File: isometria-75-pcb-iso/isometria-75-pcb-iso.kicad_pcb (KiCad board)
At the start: 2 copper layers, 308.3 x 123 mm, 320 parts, among them J101 USB, J102 SPI, J103 Conn_01x01_Male, Q101 AO3400A, SW101 RST, SW102 BOOT, SW201 Rotary_Encoder_Switch, U101 XC6206P332MR, U102 STM32F072CBTx, U301 74LVC1G125

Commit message: matched usb trace length
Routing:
- net GND: track 804.1 -> 802.0 mm, vias 24 -> 23
- net USB-D-: track 21.5 -> 23.0 mm
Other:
- net class USB: trace_width 0.254 -> 0.1905
- rule trace_min: 0.254 -> 0.127

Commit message: some minor routing improvements
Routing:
- net ROW0: track 424.0 -> 427.9 mm
- net COL4: track 211.2 -> 209.9 mm
- net SPI_RES: track 24.3 -> 25.3 mm
- net LED-: track 1894.4 -> 1895.4 mm
- net COL1: track 255.9 -> 255.2 mm
- net COL6: track 175.1 -> 174.4 mm
- net COL3: track 232.7 -> 232.0 mm
- net COL2: track 244.5 -> 243.8 mm
- net COL5: track 163.4 -> 162.7 mm
- net COL12: track 196.2 -> 195.7 mm
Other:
- net class Power: trace_width 0.3048 -> 0.508

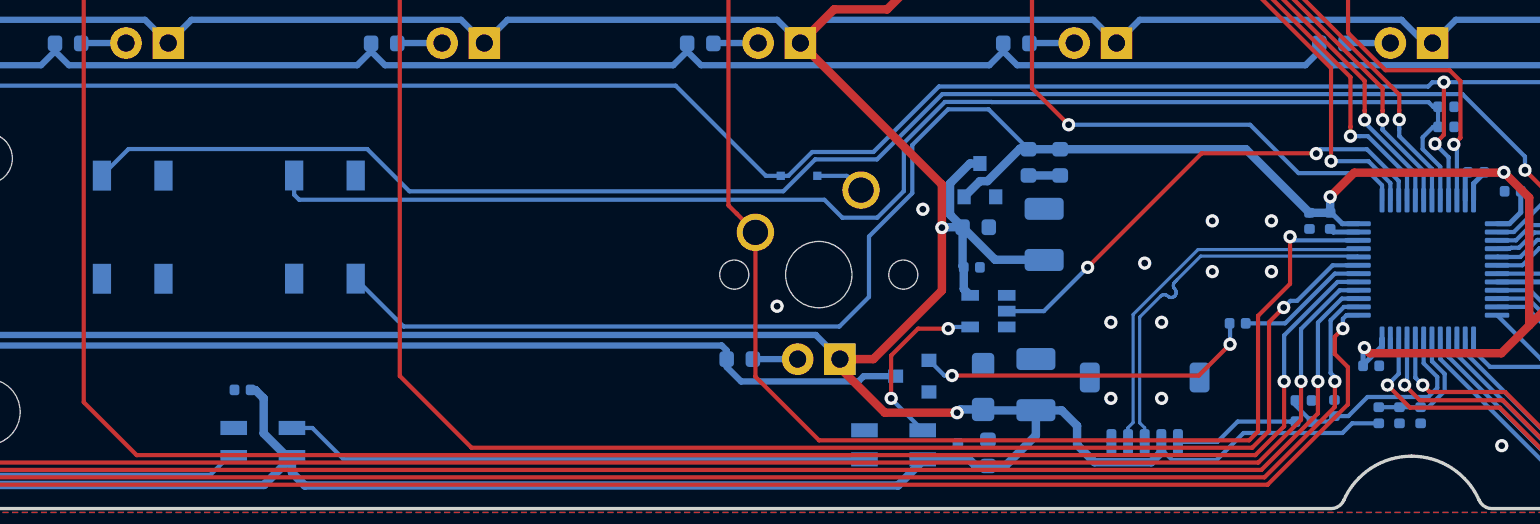
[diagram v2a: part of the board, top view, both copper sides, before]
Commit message: rerouted some traces
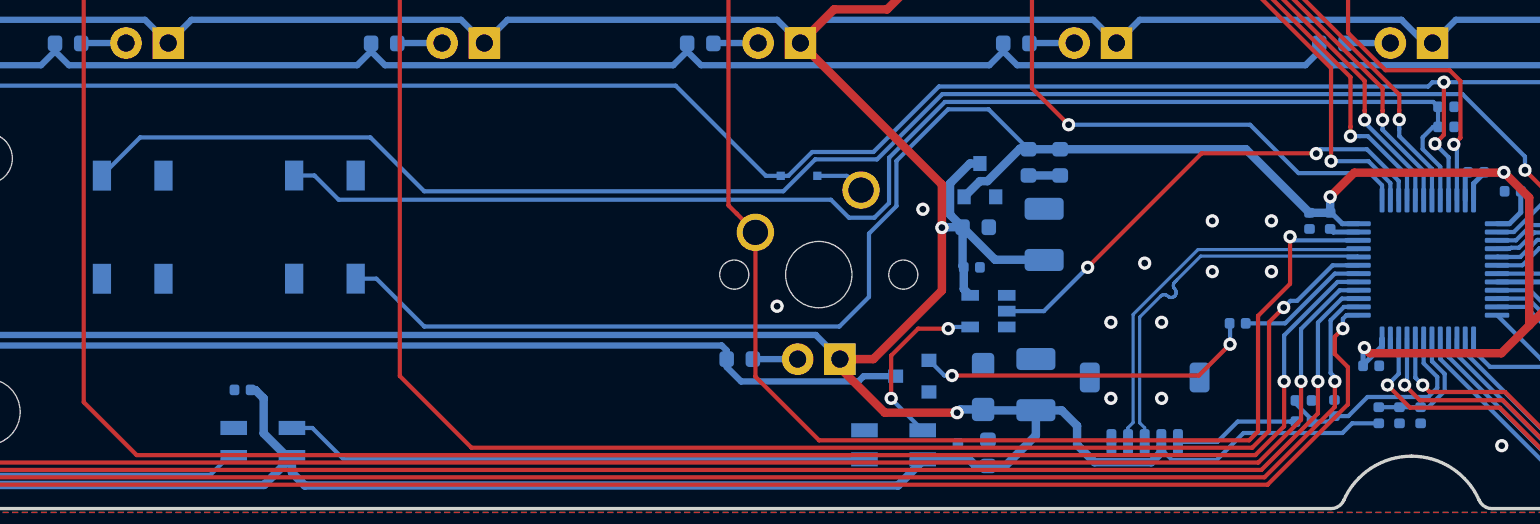
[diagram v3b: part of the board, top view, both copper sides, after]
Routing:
- net /BOOT: track 81.8 -> 81.0 mm
- net /RST: track 103.4 -> 104.0 mm
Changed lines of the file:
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@@
     (thickness 1.6)
     (drawings 37)
-    (tracks 2473)
+    (tracks 2471)
     (zones 0)
     (modules 320)
@@
   (segment (start 131.2672 94.1324) (end 133.221101 92.178499) (width 0.508) (layer B.Cu) (net 2))
   (segment (start 133.221101 92.178499) (end 133.694999 92.178499) (width 0.508) (layer B.Cu) (net 2))
-  (segment (start 131.3309 89.8144) (end 133.731 92.2145) (width 0.254) (layer B.Cu) (net 2))
-  (segment (start 128.892264 89.8144) (end 131.3309 89.8144) (width 0.254) (layer B.Cu) (net 2))
-  (segment (start 126.746 91.960664) (end 128.892264 89.8144) (width 0.254) (layer B.Cu) (net 2))
-  (segment (start 126.746 94.853116) (end 126.746 91.960664) (width 0.254) (layer B.Cu) (net 2))
-  (segment (start 124.1425 97.456616) (end 126.746 94.853116) (width 0.254) (layer B.Cu) (net 2))
-  (segment (start 124.1425 101.092) (end 124.1425 97.456616) (width 0.254) (layer B.Cu) (net 2))
-  (segment (start 122.3645 102.87) (end 124.1425 101.092) (width 0.254) (layer B.Cu) (net 2))
-  (segment (start 93.2875 99.994) (end 96.1635 102.87) (width 0.254) (layer B.Cu) (net 2))
-  (segment (start 96.1635 102.87) (end 122.3645 102.87) (width 0.254) (layer B.Cu) (net 2))
   (via (at 153.923998 104.14) (size 0.8) (drill 0.4) (layers F.Cu B.Cu) (net 2))
   (segment (start 153.843 104.220998) (end 153.923998 104.14) (width 0.3048) (layer B.Cu) (net 2))
@@
   (segment (start 168.656 101.473) (end 169.8498 102.6668) (width 0.508) (layer B.Cu) (net 2))
   (segment (start 179.5272 102.6668) (end 185.618 108.7576) (width 0.508) (layer B.Cu) (net 2))
+  (segment (start 131.3309 89.8144) (end 133.731 92.2145) (width 0.254) (layer B.Cu) (net 2))
+  (segment (start 125.7935 92.913164) (end 128.892264 89.8144) (width 0.254) (layer B.Cu) (net 2))
+  (segment (start 124.1425 97.282) (end 125.7935 95.631) (width 0.254) (layer B.Cu) (net 2))
+  (segment (start 94.533 99.994) (end 97.409 102.87) (width 0.254) (layer B.Cu) (net 2))
+  (segment (start 93.2875 99.994) (end 94.533 99.994) (width 0.254) (layer B.Cu) (net 2))
+  (segment (start 125.7935 95.631) (end 125.7935 92.913164) (width 0.254) (layer B.Cu) (net 2))
+  (segment (start 97.409 102.87) (end 122.3645 102.87) (width 0.254) (layer B.Cu) (net 2))
+  (segment (start 128.892264 89.8144) (end 131.3309 89.8144) (width 0.254) (layer B.Cu) (net 2))
+  (segment (start 122.3645 102.87) (end 124.1425 101.092) (width 0.254) (layer B.Cu) (net 2))
+  (segment (start 124.1425 101.092) (end 124.1425 97.282) (width 0.254) (layer B.Cu) (net 2))
   (segment (start 162.634 98.191) (end 161.8965 98.191) (width 0.254) (layer B.Cu) (net 3))
   (segment (start 162.721586 98.15851) (end 162.66649 98.15851) (width 0.254) (layer B.Cu) (net 3))
@@
   (segment (start 157.984 104.955064) (end 157.984 103.6035) (width 0.254) (layer B.Cu) (net 220))
   (segment (start 157.775937 107.719) (end 158.747608 106.747329) (width 0.254) (layer B.Cu) (net 220))
-  (segment (start 150.749 108.577374) (end 150.749 108.585) (width 0.254) (layer B.Cu) (net 221))
-  (segment (start 149.779 107.607374) (end 150.749 108.577374) (width 0.254) (layer B.Cu) (net 221))
-  (segment (start 149.779 107.315) (end 149.779 107.607374) (width 0.254) (layer B.Cu) (net 221))
   (segment (start 151.7904 108.585) (end 152.1206 108.2548) (width 0.254) (layer B.Cu) (net 221))
   (segment (start 150.749 108.585) (end 151.7904 108.585) (width 0.254) (layer B.Cu) (net 221))
@@
   (segment (start 157.759814 107.10649) (end 158.303097 106.563207) (width 0.254) (layer B.Cu) (net 221))
   (segment (start 158.303097 105.902795) (end 157.484 105.083698) (width 0.254) (layer B.Cu) (net 221))
+  (segment (start 150.749 108.458) (end 150.749 108.585) (width 0.254) (layer B.Cu) (net 221))
+  (segment (start 149.779 107.315) (end 149.779 107.488) (width 0.254) (layer B.Cu) (net 221))
+  (segment (start 149.779 107.488) (end 150.749 108.458) (width 0.254) (layer B.Cu) (net 221))
   (segment (start 146.304 108.585) (end 149.484 108.585) (width 0.254) (layer B.Cu) (net 222))
   (segment (start 149.484 108.585) (end 149.779 108.585) (width 0.254) (layer B.Cu) (net 222))
@@
   (segment (start 166.1541 96.0501) (end 163.576 93.472) (width 0.254) (layer F.Cu) (net 226))
   (segment (start 166.1541 99.4283) (end 166.1541 96.0501) (width 0.254) (layer F.Cu) (net 226))
-  (segment (start 96.52 94.742) (end 118.992632 94.742) (width 0.254) (layer B.Cu) (net 226))
-  (segment (start 118.992632 94.742) (end 120.910321 92.824311) (width 0.254) (layer B.Cu) (net 226))
-  (segment (start 163.576 92.6592) (end 163.576 93.472) (width 0.254) (layer B.Cu) (net 226))
-  (segment (start 79.632 92.202) (end 93.98 92.202) (width 0.254) (layer B.Cu) (net 226))
-  (segment (start 120.910321 92.824311) (end 124.625089 92.824311) (width 0.254) (layer B.Cu) (net 226))
-  (segment (start 124.625089 92.824311) (end 128.5494 88.9) (width 0.254) (layer B.Cu) (net 226))
-  (segment (start 93.98 92.202) (end 96.52 94.742) (width 0.254) (layer B.Cu) (net 226))
   (segment (start 128.5494 88.9) (end 159.8168 88.9) (width 0.254) (layer B.Cu) (net 226))
-  (segment (start 78.033 93.801) (end 79.632 92.202) (width 0.254) (layer B.Cu) (net 226))
+  (segment (start 124.625089 92.824311) (end 128.5494 88.9) (width 0.254) (layer B.Cu) (net 226))
+  (segment (start 120.910321 92.824311) (end 124.625089 92.824311) (width 0.254) (layer B.Cu) (net 226))
+  (segment (start 163.576 92.6592) (end 163.576 93.472) (width 0.254) (layer B.Cu) (net 226))
   (segment (start 159.8168 88.9) (end 163.576 92.6592) (width 0.254) (layer B.Cu) (net 226))
+  (segment (start 94.1705 91.5035) (end 97.409 94.742) (width 0.254) (layer B.Cu) (net 226))
+  (segment (start 78.033 93.801) (end 80.3305 91.5035) (width 0.254) (layer B.Cu) (net 226))
+  (segment (start 118.992632 94.742) (end 120.910321 92.824311) (width 0.254) (layer B.Cu) (net 226))
+  (segment (start 80.3305 91.5035) (end 94.1705 91.5035) (width 0.254) (layer B.Cu) (net 226))
+  (segment (start 97.409 94.742) (end 118.992632 94.742) (width 0.254) (layer B.Cu) (net 226))
   (segment (start 166.243 101.45) (end 167.64 101.45) (width 0.254) (layer B.Cu) (net 227))
   (segment (start 164.6452 101.45) (end 166.243 101.45) (width 0.254) (layer B.Cu) (net 227))
@@
   (segment (start 157.422899 92.203501) (end 157.422899 91.502101) (width 0.254) (layer B.Cu) (net 228))
   (segment (start 157.422899 91.502101) (end 158.0565 90.8685) (width 0.254) (layer B.Cu) (net 228))
-  (segment (start 158.0565 89.662) (end 158.3515 89.662) (width 0.254) (layer B.Cu) (net 228))
-  (segment (start 122.5423 96.3295) (end 124.640984 96.3295) (width 0.254) (layer B.Cu) (net 228))
-  (segment (start 121.4628 95.25) (end 122.5423 96.3295) (width 0.254) (layer B.Cu) (net 228))
-  (segment (start 89.5875 93.794) (end 89.5875 94.948) (width 0.254) (layer B.Cu) (net 228))
-  (segment (start 89.8895 95.25) (end 121.4628 95.25) (width 0.254) (layer B.Cu) (net 228))
-  (segment (start 157.7771 89.3826) (end 158.0565 89.662) (width 0.254) (layer B.Cu) (net 228))
-  (segment (start 89.5875 94.948) (end 89.8895 95.25) (width 0.254) (layer B.Cu) (net 228))
-  (segment (start 124.640984 96.3295) (end 126.238 94.732484) (width 0.254) (layer B.Cu) (net 228))
-  (segment (start 126.238 94.732484) (end 126.238 91.840032) (width 0.254) (layer B.Cu) (net 228))
-  (segment (start 128.708142 89.369889) (end 131.515022 89.369889) (width 0.254) (layer B.Cu) (net 228))
-  (segment (start 126.238 91.840032) (end 128.708142 89.369889) (width 0.254) (layer B.Cu) (net 228))
-  (segment (start 131.515022 89.369889) (end 131.527733 89.3826) (width 0.254) (layer B.Cu) (net 228))
-  (segment (start 131.527733 89.3826) (end 157.7771 89.3826) (width 0.254) (layer B.Cu) (net 228))
+  (segment (start 158.059389 89.369889) (end 158.3515 89.662) (width 0.254) (layer B.Cu) (net 228))
+  (segment (start 125.348989 92.729042) (end 128.708142 89.369889) (width 0.254) (layer B.Cu) (net 228))
+  (segment (start 125.348989 95.446879) (end 125.348989 92.729042) (width 0.254) (layer B.Cu) (net 228))
+  (segment (start 128.708142 89.369889) (end 158.059389 89.369889) (width 0.254) (layer B.Cu) (net 228))
+  (segment (start 124.466368 96.3295) (end 125.348989 95.446879) (width 0.254) (layer B.Cu) (net 228))
+  (segment (start 90.8095 93.794) (end 92.2655 95.25) (width 0.254) (layer B.Cu) (net 228))
+  (segment (start 89.5875 93.794) (end 90.8095 93.794) (width 0.254) (layer B.Cu) (net 228))
+  (segment (start 92.2655 95.25) (end 121.8565 95.25) (width 0.254) (layer B.Cu) (net 228))
+  (segment (start 121.8565 95.25) (end 122.936 96.3295) (width 0.254) (layer B.Cu) (net 228))
+  (segment (start 122.936 96.3295) (end 124.466368 96.3295) (width 0.254) (layer B.Cu) (net 228))
   (segment (start 165.468337 103.5304) (end 166.4462 103.5304) (width 0.254) (layer B.Cu) (net 229))
   (segment (start 163.628937 101.691) (end 165.468337 103.5304) (width 0.254) (layer B.Cu) (net 229))

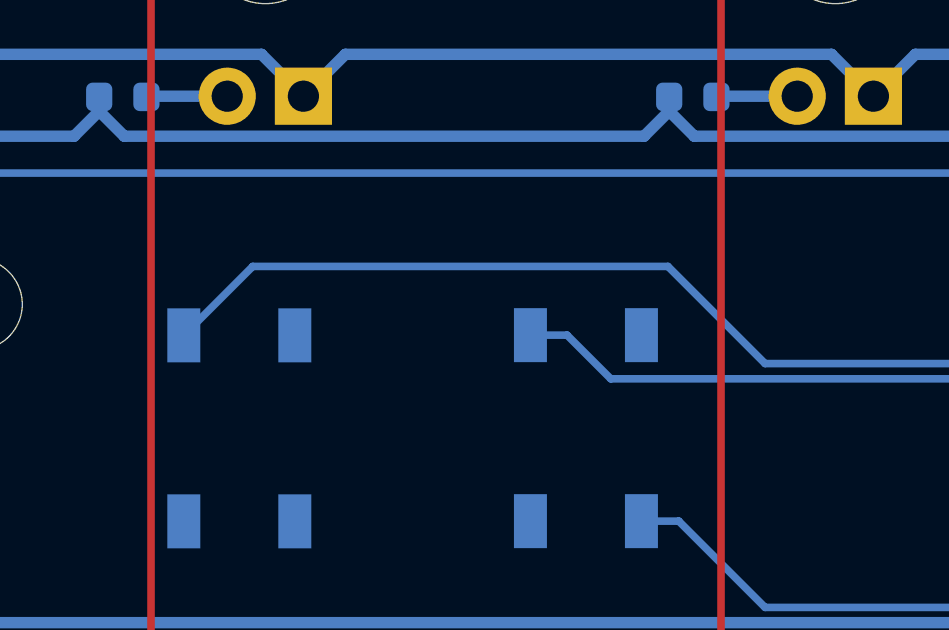
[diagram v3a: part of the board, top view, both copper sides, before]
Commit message: moved some traces
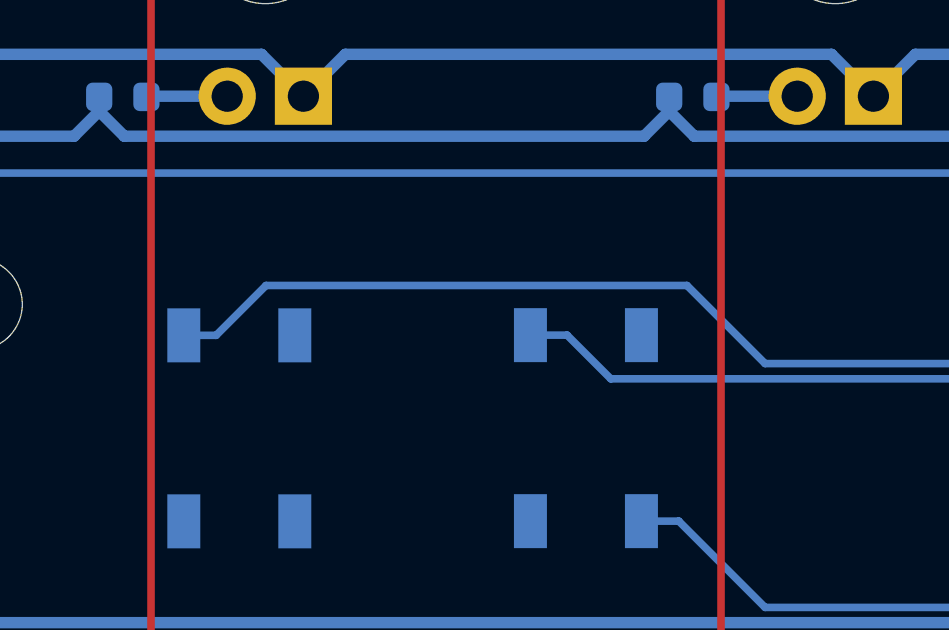
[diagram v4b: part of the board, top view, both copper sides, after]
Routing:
- net /RST: track 104.0 -> 103.5 mm
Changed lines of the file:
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@@
     (thickness 1.6)
     (drawings 37)
-    (tracks 2471)
+    (tracks 2472)
     (zones 0)
     (modules 320)
@@
   (segment (start 166.1541 96.0501) (end 163.576 93.472) (width 0.254) (layer F.Cu) (net 226))
   (segment (start 166.1541 99.4283) (end 166.1541 96.0501) (width 0.254) (layer F.Cu) (net 226))
+  (segment (start 159.8168 88.9) (end 163.576 92.6592) (width 0.254) (layer B.Cu) (net 226))
   (segment (start 128.5494 88.9) (end 159.8168 88.9) (width 0.254) (layer B.Cu) (net 226))
   (segment (start 124.625089 92.824311) (end 128.5494 88.9) (width 0.254) (layer B.Cu) (net 226))
+  (segment (start 118.992632 94.742) (end 120.910321 92.824311) (width 0.254) (layer B.Cu) (net 226))
+  (segment (start 78.033 93.801) (end 79.1095 93.801) (width 0.254) (layer B.Cu) (net 226))
   (segment (start 120.910321 92.824311) (end 124.625089 92.824311) (width 0.254) (layer B.Cu) (net 226))
+  (segment (start 80.772 92.1385) (end 94.8055 92.1385) (width 0.254) (layer B.Cu) (net 226))
   (segment (start 163.576 92.6592) (end 163.576 93.472) (width 0.254) (layer B.Cu) (net 226))
-  (segment (start 159.8168 88.9) (end 163.576 92.6592) (width 0.254) (layer B.Cu) (net 226))
-  (segment (start 94.1705 91.5035) (end 97.409 94.742) (width 0.254) (layer B.Cu) (net 226))
-  (segment (start 78.033 93.801) (end 80.3305 91.5035) (width 0.254) (layer B.Cu) (net 226))
-  (segment (start 118.992632 94.742) (end 120.910321 92.824311) (width 0.254) (layer B.Cu) (net 226))
-  (segment (start 80.3305 91.5035) (end 94.1705 91.5035) (width 0.254) (layer B.Cu) (net 226))
+  (segment (start 79.1095 93.801) (end 80.772 92.1385) (width 0.254) (layer B.Cu) (net 226))
+  (segment (start 94.8055 92.1385) (end 97.409 94.742) (width 0.254) (layer B.Cu) (net 226))
   (segment (start 97.409 94.742) (end 118.992632 94.742) (width 0.254) (layer B.Cu) (net 226))
   (segment (start 166.243 101.45) (end 167.64 101.45) (width 0.254) (layer B.Cu) (net 227))

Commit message: improved routing in a few places
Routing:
- net COL3: track 232.0 -> 226.4 mm
- net COL11: track 190.0 -> 187.3 mm
- net COL2: track 243.8 -> 241.3 mm
- net COL4: track 209.9 -> 207.5 mm
- net COL7: track 131.3 -> 129.2 mm
- net COL6: track 174.4 -> 172.9 mm
- net COL13: track 214.6 -> 213.2 mm
- net COL0: track 280.5 -> 279.3 mm
- net Net-(D316-Pad1): track 43.8 -> 44.8 mm
- net +5V: track 2694.4 -> 2693.7 mm
- net COL1: track 255.2 -> 254.5 mm
- net chgsense: track 7.57 -> 8.13 mm
- net COL8: track 117.3 -> 116.8 mm
